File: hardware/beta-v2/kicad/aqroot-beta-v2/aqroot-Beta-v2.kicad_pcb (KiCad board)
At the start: 6 copper layers, 72 x 148 mm, 324 parts, among them J1 FH69-50S-0.5SH, J2 Molex_5025700893, J3 USB_C_Receptacle_USB2.0_16P, J4 JST-PH-2 BATTERY, J5 COMMUNITY_PORT_1x24, J6 JST-PH-2 SPEAKER, J7 BM02B-ACHSS-GAN-ETF, J8 QWIIC_STEMMA_QT, Q1 AO3400A, Q10 2N7002, Q2 NTMD4820N, Q3 NTMD4820N, Q4 BSS138, Q5 AO3401A, Q6 BSS138, Q7 BSS138, Q8 BSS138, Q9 BSS138, SW1 BOOT, SW2 UP, SW3 DOWN, SW4 LEFT, SW5 RIGHT, SW6 A_SELECT, SW7 B_BACK, SW9 SW_SPDT, U1 ESP32-S3-WROOM-1, U10 USBLC6-2SC6, U11 BQ25185, U12 TPS63020, U13 TPS61023, U14 MAX17048, U16 TCA4307DGKR, U17 TPS61169DCKR, U18 LTC4368-1, U19 TLV7032, U2 PCAL9535APW, U20 TPS22950C, U21 TPS61023, U22 TPS22950C, U23 PCAL9535APW, U3 PCAL9535APW, U4 BMI270, U5 MAX98357A, U6 TSOP38238, U7 E07-400M10S, U8 E22-900M22S, U9 ST25R3916-AQET, Y1 27.12MHz 10pF 3225-4P

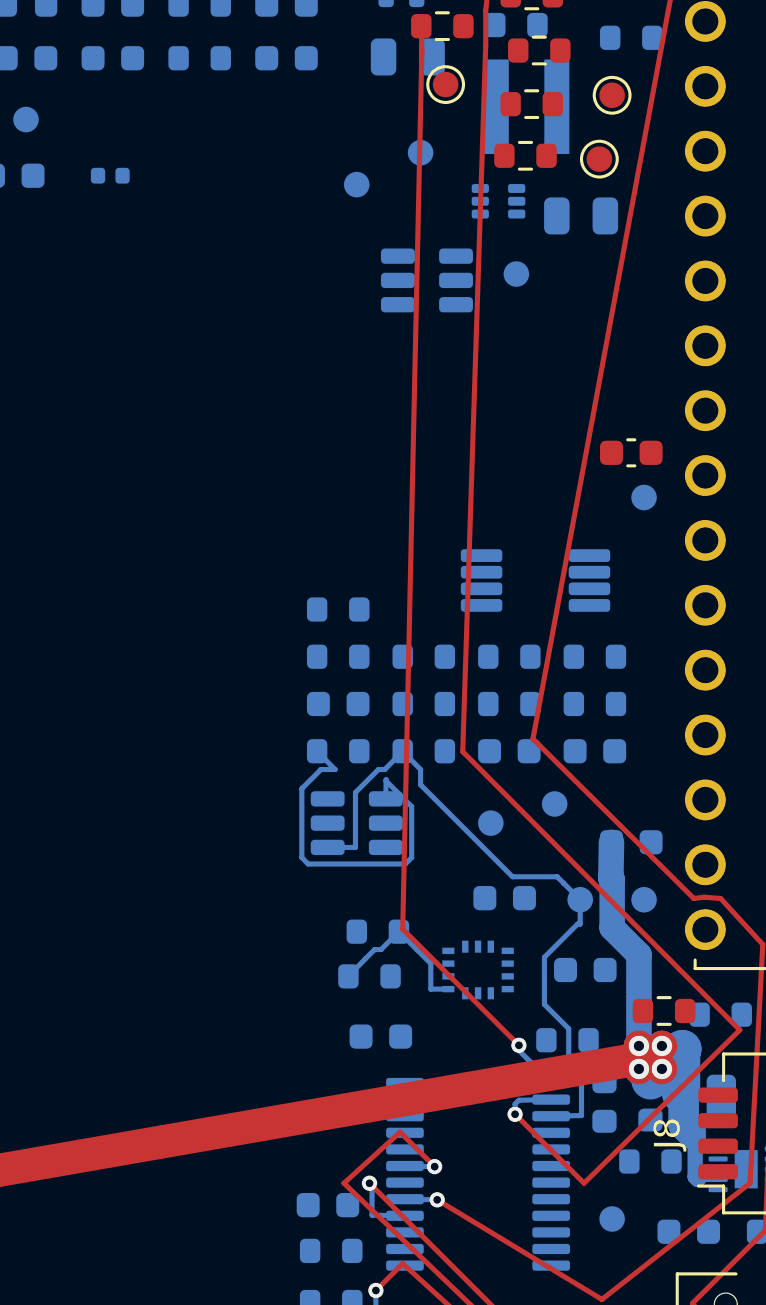
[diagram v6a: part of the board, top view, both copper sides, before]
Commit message: FBV2-P2-025: D-323 EIGHTEENTH REST-OF-BOARD INCREMENTAL INCREMENT ROUTED + PROMOTED — the accelerometer/add-on presence-detect ACC_DETECT_N (R64.1 divider F.Cu / R129.2 series B.Cu / U3.17 PCAL expander GPIO B.Cu), a 3-pad cross-layer net = ONE 0.60/0.30 through via (R64.1<->R129.2, In1/In4 re-poured) + ONE same-layer B.Cu run (R129.2<->U3.17), a genuine functional low-speed CMOS detect input in an OPEN region whose realized copper clears BAT_PROTECTED_P by 3.8831 mm (zero D-269 involvement); PROMOTED after the cleaner-class DISP_BL_CTL_STRAP (display backlight-control strap U1.16/TP2.1/R108.1/R109.1) hit a CHARACTERIZED boxed-MCU-pocket local wall (all three MST edges NO_PATH at 0.200 mm even on the fine grid) and after BTN_B_N (button SW7.1/R9.2/U2.18) routed ALL OK but FAILED the real full-board gate on connectivity (SW7 is a 4-pin tact switch whose two terminals share pad "1" 7.96 mm apart -> the per-ref MST leaves the second terminal open; a whole-duplicate-ref-button-family framework limit, NOT a copper casualty, AUTH never touched); a governed CTO ACCEPT + PROMOTE, ZERO router-logic change.
AUTH sha a861e30e... -> a7bf8bdc11f1bc39303c6f6b6c801e3a4a575add64596cc4be20745c57f9f626; tracks 759->781 (+22: 3 F.Cu + 19 B.Cu 0.200 mm); vias 67->68 (+1 through via @57.900,38.800, the first new via since D-316); ratsnest 667->665 (-2); journal 114->116 (+2 REST_INC). Gate PASS every check (0 Phase-A altered, 22 trk + 1 via all target-net, only In1/In4 GND planes re-poured, open_edges 2->0, 0 prior pairs regressed, no new/worse DRC, unconnected 499->499). New G35; router_regression ALL PASS G1-G35 twice (deterministic); new incremental_probe_023.py PASS; _006..022 + phaseB_bringup_probe_005 (781/68/116; 26 routed rest, 138 unrouted) PASS. Probe via-total generalization: no-via probes 018-022 board-total pin generalized from hard-coded 67 to len(via)==EXPECT_VIAS keeping per-net i_via==0; probe_023 aligned (per-net i_via==1) -- ZERO contract weakened. live_fingerprint bu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
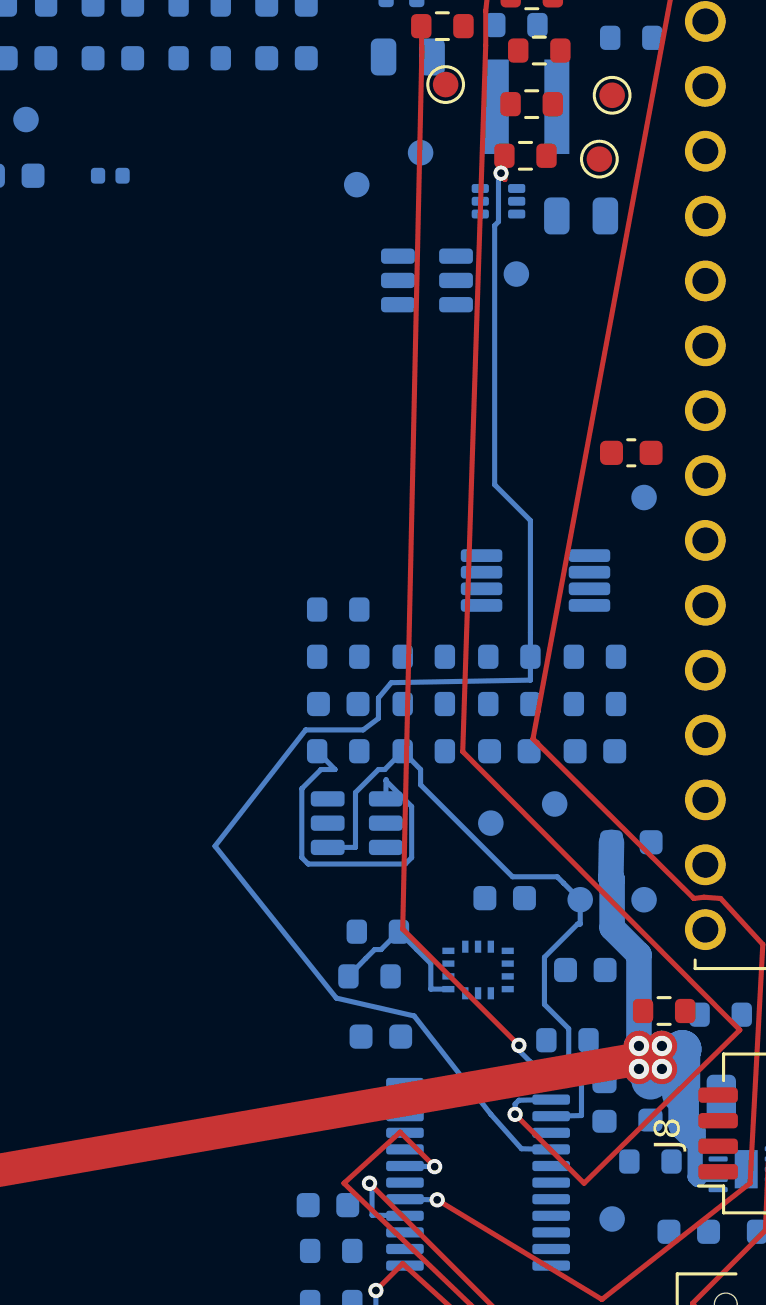
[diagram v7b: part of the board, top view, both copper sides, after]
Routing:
- net /ACC_DETECT_N: track 0.00 -> 56.2 mm, vias 0 -> 1
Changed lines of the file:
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@@
+	)
+	(segment
+		(start 57.9 38.9)
+		(end 57.9 38.8)
+		(width 0.2)
+		(layer "F.Cu")
+		(net "/ACC_DETECT_N")
+	)
+	(segment
+		(start 58.05 39.05)
+		(end 57.9 38.9)
+		(width 0.2)
+		(layer "F.Cu")
+		(net "/ACC_DETECT_N")
+	)
+	(segment
+		(start 58.031538 38.119292)
+		(end 58.05 39.05)
+		(width 0.2)
+		(layer "F.Cu")
+		(net "/ACC_DETECT_N")
+	)
+	(via
+		(at 57.9 38.8)
+		(size 0.6)
+		(drill 0.3)
+		(layers "F.Cu" "B.Cu")
+		(net "/ACC_DETECT_N")
+	)
+	(segment
+		(start 57.8 38.9)
+		(end 57.9 38.8)
+		(width 0.2)
+		(layer "B.Cu")
+		(net "/ACC_DETECT_N")
+	)
+	(segment
+		(start 59.8625 77.025)
+		(end 58.7 77)
+		(width 0.2)
+		(layer "B.Cu")
+		(net "/ACC_DETECT_N")
+	)
+	(segment
+		(start 57.5 75.65)
+		(end 58.7 77)
+		(width 0.2)
+		(layer "B.Cu")
+		(net "/ACC_DETECT_N")
+	)
+	(segment
+		(start 59.05 58.65)
+		(end 53.6 58.75)
+		(width 0.2)
+		(layer "B.Cu")
+		(net "/ACC_DETECT_N")
+	)
+	(segment
+		(start 53.1 60.15)
+		(end 52.5 60.6)
+		(width 0.2)
+		(layer "B.Cu")
+		(net "/ACC_DETECT_N")
+	)
+	(segment
+		(start 59.05 56.8)
+		(end 59.05 52.4)
+		(width 0.2)
+		(layer "B.Cu")
+		(net "/ACC_DETECT_N")
+	)
+	(segment
+		(start 46.7 65.15)
+		(end 51.45 71.1)
+		(width 0.2)
+		(layer "B.Cu")
+		(net "/ACC_DETECT_N")
+	)
+	(segment
+		(start 53.1 59.35)
+		(end 53.1 60.15)
+		(width 0.2)
+		(layer "B.Cu")
+		(net "/ACC_DETECT_N")
+	)
+	(segment
+		(start 57.8 40.7)
+		(end 57.8 38.9)
+		(width 0.2)
+		(layer "B.Cu")
+		(net "/ACC_DETECT_N")
+	)
+	(segment
+		(start 59.05 57.735)
+		(end 59.05 58.65)
+		(width 0.2)
+		(layer "B.Cu")
+		(net "/ACC_DETECT_N")
+	)
+	(segment
+		(start 53.6 58.75)
+		(end 53.1 59.35)
+		(width 0.2)
+		(layer "B.Cu")
+		(net "/ACC_DETECT_N")
+	)
+	(segment
+		(start 52.5 60.6)
+		(end 50.25 60.6)
+		(width 0.2)
+		(layer "B.Cu")
+		(net "/ACC_DETECT_N")
+	)
+	(segment
+		(start 59.05 57.735)
+		(end 59.05 56.8)
+		(width 0.2)
+		(layer "B.Cu")
+		(net "/ACC_DETECT_N")
+	)
+	(segment
+		(start 50.25 60.6)
+		(end 46.7 65.15)
+		(width 0.2)
+		(layer "B.Cu")
+		(net "/ACC_DETECT_N")
+	)
+	(segment
+		(start 57.65 51)
+		(end 57.65 40.85)
+		(width 0.2)
+		(layer "B.Cu")
+		(net "/ACC_DETECT_N")
+	)
+	(segment
+		(start 59.05 52.4)
+		(end 57.65 51)
+		(width 0.2)
+		(layer "B.Cu")
+		(net "/ACC_DETECT_N")
+	)
+	(segment
+		(start 51.45 71.1)
+		(end 54.5 71.8)
+		(width 0.2)
+		(layer "B.Cu")
+		(net "/ACC_DETECT_N")
+	)
+	(segment
+		(start 54.5 71.8)
+		(end 57.5 75.65)
+		(width 0.2)
+		(layer "B.Cu")
+		(net "/ACC_DETECT_N")
+	)
+	(segment
+		(start 57.65 40.85)
+		(end 57.8 40.7)
+		(width 0.2)
+		(layer "B.Cu")
+		(net "/ACC_DETECT_N")
 	)
 	(segment

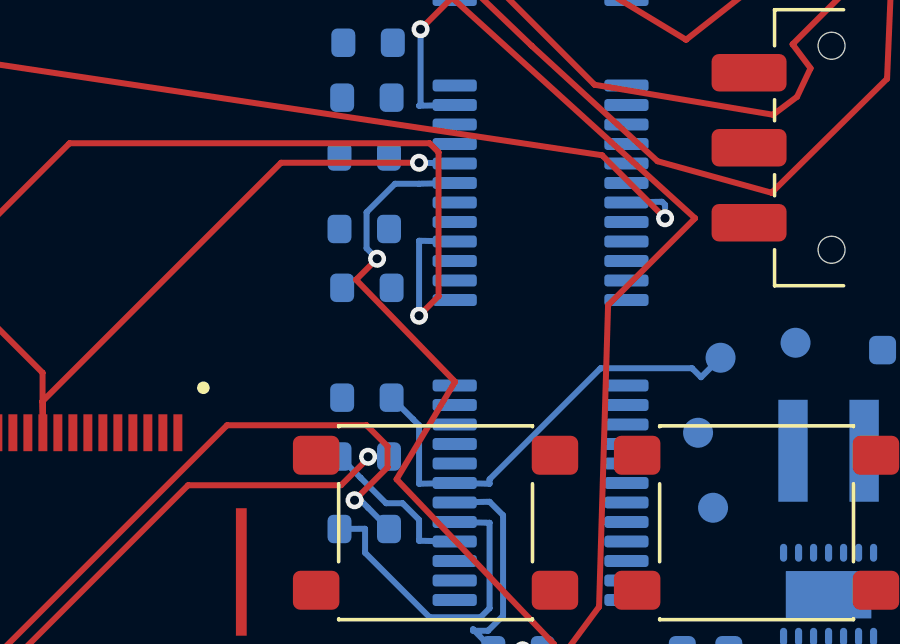
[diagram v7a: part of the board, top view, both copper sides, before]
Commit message: FBV2-P2-027: D-325 DUPLICATE-REF MST FRAMEWORK FIX + BTN_B_N PROMOTED (nineteenth rest-of-board increment, the FIRST framework-dependent one) — a bounded, generic, deterministic change lets the MST and the gate treat a footprint's TWO same-numbered physical lands as distinct nodes, unlocking the whole SWx user-button family; the navigation/boot button BTN_B_N (SW7.1 F.Cu / R9.2 pull-up B.Cu / U2.18 expander B.Cu) then routed, PASSED the real full-board gate, and was PROMOTED. ROOT CAUSE: SW7 (Button_Switch_SMD:SW_SPST_PTS645Sx43SMTR92) is a 4-pin tact switch whose two mechanically-linked terminals BOTH carry pad number "1" on BTN_B_N at (49.520,96.750) and (57.480,96.750) 7.96 mm apart; qrouter.QBoard._scan keys self.pads[(net,"REF.NUM")] so the second land overwrote the first and was invisible to net_pads()/the MST (D-323 gate FAIL open_edges 2->1), and cmd_gate.net_open_edges() ref-deduped the two lands in its own cluster count. FIX (in incremental_router.py ONLY; qrouter.py UNTOUCHED so every G-contract that routes through QBoard stays byte-identical): physical_net_pads() keys MST nodes by stable PHYSICAL identity (ref,x,y) — ordinary unique-pad nets return the exact net_pads() dict objects, byte-identical; net_open_edges() rewritten as a physical-pad union-find that counts copper clusters over physical lands, matching KiCad's own ratsnest (4 lands -> 3 edges). BTN_B_N MST hubs on R9.2 -> BOTH SW7.1 lands (two 0.60/0.30 Default THROUGH vias at (48.300,96.750) and (56.300,95.600) in the OPEN south button field, In1/In4 re-poured once) + one same-layer B.Cu run R9.2->U2.18; 19 trk (3 F.Cu + 16 B.Cu) + 2 vias. GATE PASS all 10: all four physical pads one copper cluster (open_edges 3->0, both SW7.1 lands driven), ratsnest 665->662 (-3), no new/worse DRC (clearance 0), unconnected_items 499->499; realized copper 10.68 mm clear of BAT_PROTECTED_P (zero D-269), both vias >= 2.915 mm from every barrel. AUTH a7bf8bdc...(781/68/665/116) -> 35d32343...(800/70/662/119). TEST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
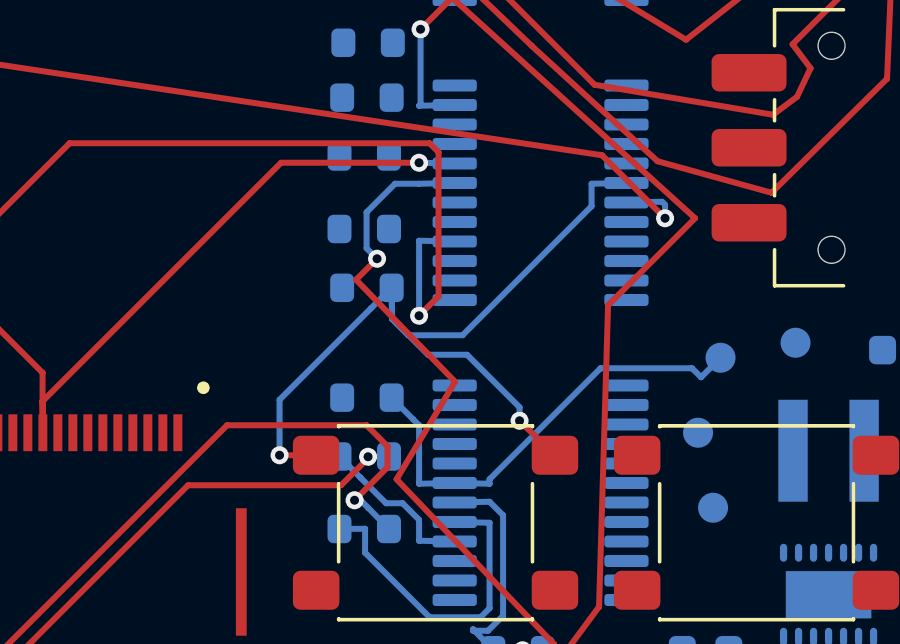
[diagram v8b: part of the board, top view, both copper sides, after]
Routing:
- net /08_BUTTONS_EXPANDERS/BTN_B_N: track 0.00 -> 28.6 mm, vias 0 -> 2
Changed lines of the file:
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@@
+	)
+	(segment
+		(start 57.48 96.75)
+		(end 56.5 95.8)
+		(width 0.2)
+		(layer "F.Cu")
+		(net "/08_BUTTONS_EXPANDERS/BTN_B_N")
+	)
+	(segment
+		(start 49.52 96.75)
+		(end 48.3 96.75)
+		(width 0.2)
+		(layer "F.Cu")
+		(net "/08_BUTTONS_EXPANDERS/BTN_B_N")
+	)
+	(segment
+		(start 56.5 95.8)
+		(end 56.3 95.6)
+		(width 0.2)
+		(layer "F.Cu")
+		(net "/08_BUTTONS_EXPANDERS/BTN_B_N")
+	)
+	(via
+		(at 48.3 96.75)
+		(size 0.6)
+		(drill 0.3)
+		(layers "F.Cu" "B.Cu")
+		(net "/08_BUTTONS_EXPANDERS/BTN_B_N")
+	)
+	(via
+		(at 56.3 95.6)
+		(size 0.6)
+		(drill 0.3)
+		(layers "F.Cu" "B.Cu")
+		(net "/08_BUTTONS_EXPANDERS/BTN_B_N")
+	)
+	(segment
+		(start 53.25 93.4)
+		(end 54.55 93.4)
+		(width 0.2)
+		(layer "B.Cu")
+		(net "/08_BUTTONS_EXPANDERS/BTN_B_N")
+	)
+	(segment
+		(start 58.7 88.45)
+		(end 58.7 87.7)
+		(width 0.2)
+		(layer "B.Cu")
+		(net "/08_BUTTONS_EXPANDERS/BTN_B_N")
+	)
+	(segment
+		(start 52.6 92.75)
+		(end 54.4 92.75)
+		(width 0.2)
+		(layer "B.Cu")
+		(net "/08_BUTTONS_EXPANDERS/BTN_B_N")
+	)
+	(segment
+		(start 51.35 91.85)
+		(end 48.3 94.9)
+		(width 0.2)
+		(layer "B.Cu")
+		(net "/08_BUTTONS_EXPANDERS/BTN_B_N")
+	)
+	(segment
+		(start 48.3 94.9)
+		(end 48.3 96.75)
+		(width 0.2)
+		(layer "B.Cu")
+		(net "/08_BUTTONS_EXPANDERS/BTN_B_N")
+	)
+	(segment
+		(start 52.05 92.1)
+		(end 52.05 92.2)
+		(width 0.2)
+		(layer "B.Cu")
+		(net "/08_BUTTONS_EXPANDERS/BTN_B_N")
+	)
+	(segment
+		(start 54.4 92.75)
+		(end 58.7 88.45)
+		(width 0.2)
+		(layer "B.Cu")
+		(net "/08_BUTTONS_EXPANDERS/BTN_B_N")
+	)
+	(segment
+		(start 52.05 92.1)
+		(end 52.05 92.2)
+		(width 0.2)
+		(layer "B.Cu")
+		(net "/08_BUTTONS_EXPANDERS/BTN_B_N")
+	)
+	(segment
+		(start 54.55 93.4)
+		(end 56.3 95.15)
+		(width 0.2)
+		(layer "B.Cu")
+		(net "/08_BUTTONS_EXPANDERS/BTN_B_N")
+	)
+	(segment
+		(start 52.05 92.2)
+		(end 52.6 92.75)
+		(width 0.2)
+		(layer "B.Cu")
+		(net "/08_BUTTONS_EXPANDERS/BTN_B_N")
+	)
+	(segment
+		(start 52.05 92.2)
+		(end 53.25 93.4)
+		(width 0.2)
+		(layer "B.Cu")
+		(net "/08_BUTTONS_EXPANDERS/BTN_B_N")
+	)
+	(segment
+		(start 52.035594 91.169035)
+		(end 51.35 91.85)
+		(width 0.2)
+		(layer "B.Cu")
+		(net "/08_BUTTONS_EXPANDERS/BTN_B_N")
+	)
+	(segment
+		(start 59.8625 87.675)
+		(end 58.7 87.7)
+		(width 0.2)
+		(layer "B.Cu")
+		(net "/08_BUTTONS_EXPANDERS/BTN_B_N")
+	)
+	(segment
+		(start 52.035594 91.169035)
+		(end 52.05 92.1)
+		(width 0.2)
+		(layer "B.Cu")
+		(net "/08_BUTTONS_EXPANDERS/BTN_B_N")
+	)
+	(segment
+		(start 52.035594 91.169035)
+		(end 52.05 92.1)
+		(width 0.2)
+		(layer "B.Cu")
+		(net "/08_BUTTONS_EXPANDERS/BTN_B_N")
+	)
+	(segment
+		(start 56.3 95.15)
+		(end 56.3 95.6)
+		(width 0.2)
+		(layer "B.Cu")
+		(net "/08_BUTTONS_EXPANDERS/BTN_B_N")
 	)
 	(segment
